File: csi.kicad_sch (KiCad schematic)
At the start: 61 parts, among them J10 Conn_FFC_WE_68715014522, J11 Conn_FFC_WE_68715014522, U43 PI4MSD5V9548AZDEX, U44 AP22615A_TSOT26, U45 AP22615A_TSOT26, U46 AP22615A_TSOT26, U47 AP22615A_TSOT26, U48 NTS0102_XSON, U49 NTS0102_XSON

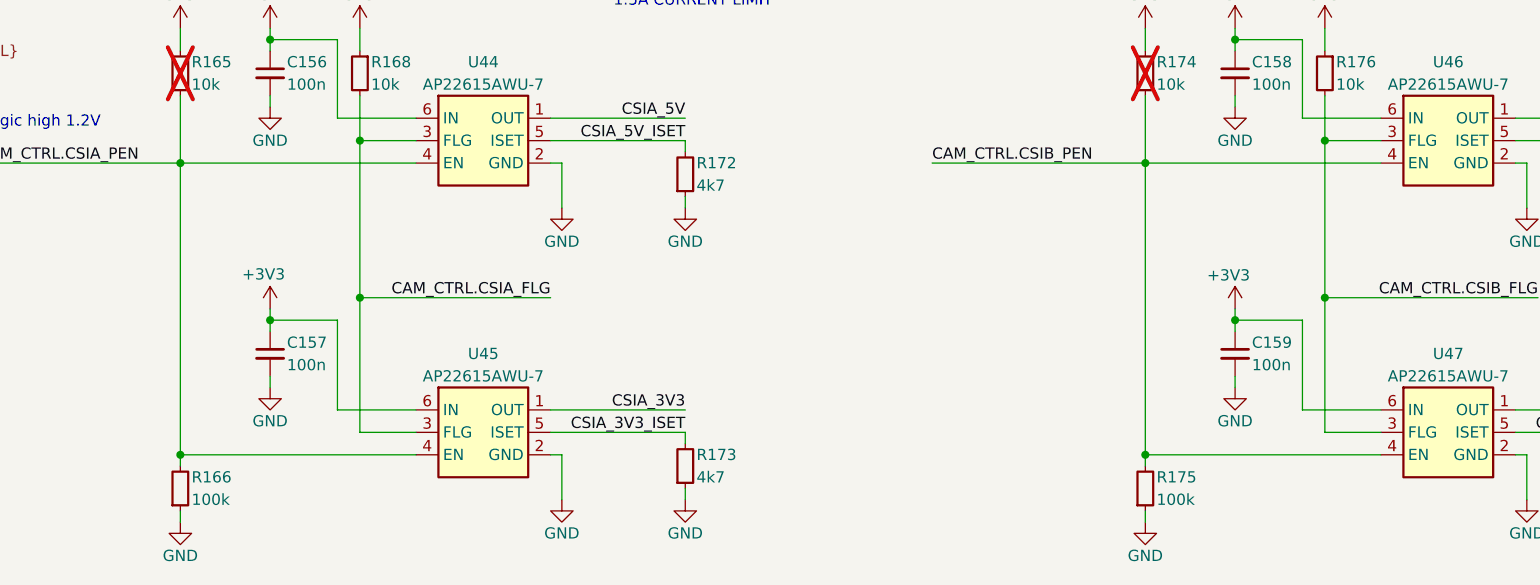
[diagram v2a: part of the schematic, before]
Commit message: [#83396] Implement small post review fixes eg. correct LED resistor values, update sheet table, delete four wire connections
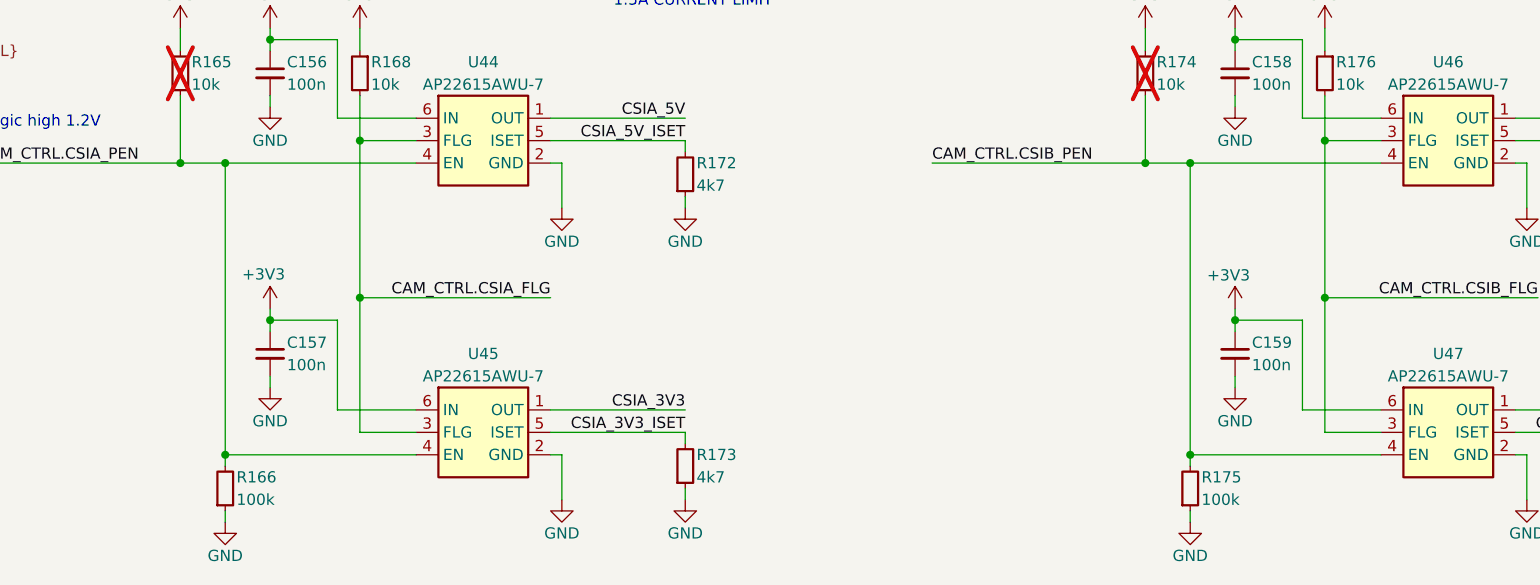
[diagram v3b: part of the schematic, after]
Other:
- moved on the sheet: R166, R175
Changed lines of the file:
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@@
 	)
 	(junction
-		(at 201.93 248.92)
+		(at 207.01 248.92)
 		(diameter 0)
 		(color 0 0 0 0)
@@
 	)
 	(junction
+		(at 97.79 215.9)
+		(diameter 0)
+		(color 0 0 0 0)
+	)
+	(junction
 		(at 349.25 154.94)
 		(diameter 0)
@@
 	)
 	(junction
-		(at 92.71 248.92)
+		(at 97.79 248.92)
 		(diameter 0)
 		(color 0 0 0 0)
@@
 	)
 	(junction
+		(at 207.01 215.9)
+		(diameter 0)
+		(color 0 0 0 0)
+	)
+	(junction
 		(at 284.48 106.68)
 		(diameter 0)
@@
 	(wire
 		(pts
-			(xy 201.93 215.9) (xy 201.93 248.92)
+			(xy 207.01 215.9) (xy 207.01 248.92)
 		)
 		(stroke
@@
 	(wire
 		(pts
-			(xy 92.71 255.27) (xy 92.71 256.54)
+			(xy 97.79 255.27) (xy 97.79 256.54)
 		)
 		(stroke
@@
 	(wire
 		(pts
-			(xy 92.71 215.9) (xy 119.38 215.9)
-		)
-		(stroke
-			(width 0)
-			(type default)
-		)
-	)
-	(wire
-		(pts
 			(xy 102.87 200.66) (xy 102.87 201.93)
 		)
@@
 	(wire
 		(pts
-			(xy 201.93 255.27) (xy 201.93 256.54)
+			(xy 207.01 255.27) (xy 207.01 256.54)
 		)
 		(stroke
@@
 	(wire
 		(pts
-			(xy 92.71 215.9) (xy 92.71 248.92)
+			(xy 97.79 215.9) (xy 97.79 248.92)
 		)
 		(stroke
@@
 	(wire
 		(pts
-			(xy 201.93 248.92) (xy 228.6 248.92)
+			(xy 207.01 215.9) (xy 228.6 215.9)
+		)
+		(stroke
+			(width 0)
+			(type default)
+		)
+	)
+	(wire
+		(pts
+			(xy 207.01 248.92) (xy 228.6 248.92)
 		)
 		(stroke
@@
 	(wire
 		(pts
-			(xy 92.71 248.92) (xy 119.38 248.92)
+			(xy 97.79 248.92) (xy 119.38 248.92)
 		)
 		(stroke
@@
 	(wire
 		(pts
-			(xy 201.93 215.9) (xy 228.6 215.9)
+			(xy 201.93 215.9) (xy 207.01 215.9)
 		)
 		(stroke
@@
 	(wire
 		(pts
+			(xy 97.79 215.9) (xy 119.38 215.9)
+		)
+		(stroke
+			(width 0)
+			(type default)
+		)
+	)
+	(wire
+		(pts
 			(xy 372.11 226.06) (xy 372.11 227.33)
 		)
@@
 	(wire
 		(pts
-			(xy 92.71 248.92) (xy 92.71 250.19)
+			(xy 97.79 248.92) (xy 97.79 250.19)
 		)
 		(stroke
@@
 	(wire
 		(pts
-			(xy 201.93 248.92) (xy 201.93 250.19)
+			(xy 207.01 248.92) (xy 207.01 250.19)
 		)
 		(stroke
@@
 		)
 	)
+	(wire
+		(pts
+			(xy 97.79 215.9) (xy 92.71 215.9)
+		)
+		(stroke
+			(width 0)
+			(type default)
+		)
+	)
 	(bus
 		(pts
@@
 	(symbol
 		(lib_id "antmicroResistors0402:R_100k_0402")
-		(at 92.71 255.27 90)
+		(at 97.79 255.27 90)
 		(unit 1)
 		(exclude_from_sim no)
@@
 		(dnp no)
 		(property "Reference" "R166"
-			(at 93.98 251.46 90)
+			(at 99.06 251.46 90)
 			(effects
 				(font
@@
 		)
 		(property "Value" "R_100k_0402"
-			(at 105.41 234.95 0)
+			(at 110.49 234.95 0)
 			(effects
 				(font
@@
 		)
 		(property "Footprint" "antmicro-footprints:R_0402_1005Metric"
-			(at 107.95 234.95 0)
+			(at 113.03 234.95 0)
 			(effects
 				(font
@@
 		)
 		(property "Datasheet" "https://www.bourns.com/docs/product-datasheets/cr.pdf"
-			(at 110.49 234.95 0)
+			(at 115.57 234.95 0)
 			(effects
 				(font
@@
 		)
 		(property "Description" "SMD Chip Resistor, 100 kohm, ± 1%, 62.5 mW, 0402 [1005 Metric], Thick Film, General Purpose"
-			(at 92.71 255.27 0)
+			(at 97.79 255.27 0)
 			(effects
 				(font
@@
 		)
 		(property "Manufacturer" "Bourns"
-			(at 115.57 234.95 0)
+			(at 120.65 234.95 0)
 			(effects
 				(font
@@
 		)
 		(property "MPN" "CR0402-FX-1003GLF"
-			(at 113.03 234.95 0)
+			(at 118.11 234.95 0)
 			(effects
 				(font
@@
 		)
 		(property "Val" "100k"
-			(at 93.98 254 90)
+			(at 99.06 254 90)
 			(effects
 				(font
@@
 		)
 		(property "License" "Apache-2.0"
-			(at 118.11 234.95 0)
+			(at 123.19 234.95 0)
 			(effects
 				(font
@@
 		)
 		(property "Author" "Antmicro"
-			(at 120.65 234.95 0)
+			(at 125.73 234.95 0)
 			(effects
 				(font
@@
 		)
 		(property "Tolerance" "1%"
-			(at 102.87 234.95 0)
+			(at 107.95 234.95 0)
 			(effects
 				(font
@@
 	(symbol
 		(lib_id "antmicropower:GND")
-		(at 92.71 256.54 0)
+		(at 97.79 256.54 0)
 		(unit 1)
 		(exclude_from_sim no)
@@
 		(dnp no)
 		(property "Reference" "#PWR0292"
-			(at 92.71 262.89 0)
+			(at 97.79 262.89 0)
 			(effects
 				(font
@@
 		)
 		(property "Value" "GND"
-			(at 92.71 260.35 0)
+			(at 97.79 260.35 0)
 			(effects
 				(font
@@
 		)
 		(property "Footprint" ""
-			(at 101.6 264.16 0)
+			(at 106.68 264.16 0)
 			(effects
 				(font
@@
 		)
 		(property "Datasheet" ""
-			(at 101.6 269.24 0)
+			(at 106.68 269.24 0)
 			(effects
 				(font
@@
 		)
 		(property "Description" ""
-			(at 92.71 256.54 0)
+			(at 97.79 256.54 0)
 			(effects
 				(font
@@
 		)
 		(property "Author" "Antmicro"
-			(at 101.6 264.16 0)
+			(at 106.68 264.16 0)
 			(effects
 				(font
@@
 		)
 		(property "License" "Apache-2.0"
-			(at 101.6 266.7 0)
+			(at 106.68 266.7 0)
 			(effects
 				(font
@@
 	(symbol
 		(lib_id "antmicroResistors0402:R_100k_0402")
-		(at 201.93 255.27 90)
+		(at 207.01 255.27 90)
 		(unit 1)
 		(exclude_from_sim no)
@@
 		(dnp no)
 		(property "Reference" "R175"
-			(at 203.2 251.46 90)
+			(at 208.28 251.46 90)
 			(effects
 				(font
@@
 		)
 		(property "Value" "R_100k_0402"
-			(at 214.63 234.95 0)
+			(at 219.71 234.95 0)
 			(effects
 				(font
@@
 		)
 		(property "Footprint" "antmicro-footprints:R_0402_1005Metric"
-			(at 217.17 234.95 0)
+			(at 222.25 234.95 0)
 			(effects
 				(font
@@
 		)
 		(property "Datasheet" "https://www.bourns.com/docs/product-datasheets/cr.pdf"
-			(at 219.71 234.95 0)
+			(at 224.79 234.95 0)
 			(effects
 				(font
@@
 		)
 		(property "Description" "SMD Chip Resistor, 100 kohm, ± 1%, 62.5 mW, 0402 [1005 Metric], Thick Film, General Purpose"
-			(at 201.93 255.27 0)
+			(at 207.01 255.27 0)
 			(effects
 				(font
@@
 		)
 		(property "Manufacturer" "Bourns"
-			(at 224.79 234.95 0)
+			(at 229.87 234.95 0)
 			(effects
 				(font
@@
 		)
 		(property "MPN" "CR0402-FX-1003GLF"
-			(at 222.25 234.95 0)
+			(at 227.33 234.95 0)
 			(effects
 				(font
@@
 		)
 		(property "Val" "100k"
-			(at 203.2 254 90)
+			(at 208.28 254 90)
 			(effects
 				(font
@@
 		)
 		(property "License" "Apache-2.0"
-			(at 227.33 234.95 0)
+			(at 232.41 234.95 0)
 			(effects
 				(font
@@
 		)
 		(property "Author" "Antmicro"
-			(at 229.87 234.95 0)
+			(at 234.95 234.95 0)
 			(effects
 				(font
@@
 		)
 		(property "Tolerance" "1%"
-			(at 212.09 234.95 0)
+			(at 217.17 234.95 0)
 			(effects
 				(font
@@
 	(symbol
 		(lib_id "antmicropower:GND")
-		(at 201.93 256.54 0)
+		(at 207.01 256.54 0)
 		(unit 1)
 		(exclude_from_sim no)
@@
 		(dnp no)
 		(property "Reference" "#PWR0309"
-			(at 201.93 262.89 0)
+			(at 207.01 262.89 0)
 			(effects
 				(font
@@
 		)
 		(property "Value" "GND"
-			(at 201.93 260.35 0)
+			(at 207.01 260.35 0)
 			(effects
 				(font
@@
 		)
 		(property "Footprint" ""
-			(at 210.82 264.16 0)
+			(at 215.9 264.16 0)
 			(effects
 				(font
@@
 		)
 		(property "Datasheet" ""
-			(at 210.82 269.24 0)
+			(at 215.9 269.24 0)
 			(effects
 				(font
@@
 		)
 		(property "Description" ""
-			(at 201.93 256.54 0)
+			(at 207.01 256.54 0)
 			(effects
 				(font
@@
 		)
 		(property "Author" "Antmicro"
-			(at 210.82 264.16 0)
+			(at 215.9 264.16 0)
 			(effects
 				(font
@@
 		)
 		(property "License" "Apache-2.0"
-			(at 210.82 266.7 0)
+			(at 215.9 266.7 0)
 			(effects
 				(font

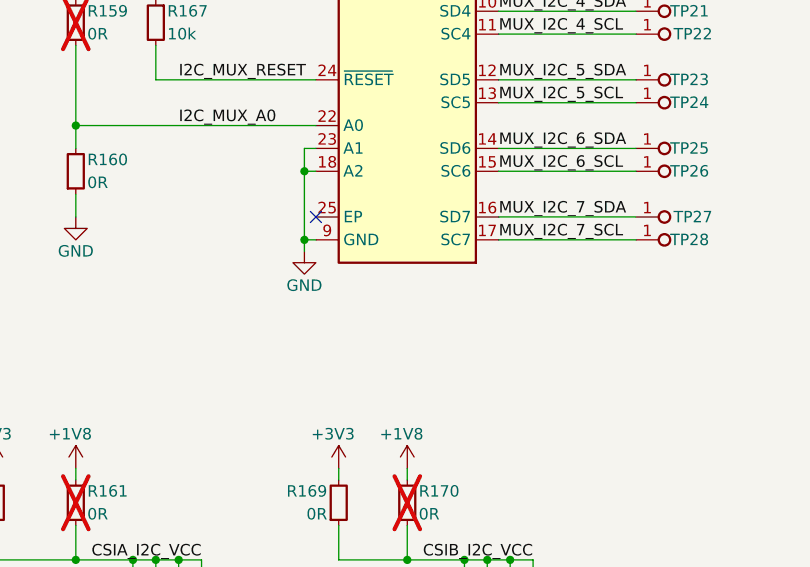
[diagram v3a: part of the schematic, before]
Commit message: [#84355] Add antmicro logo to PCB
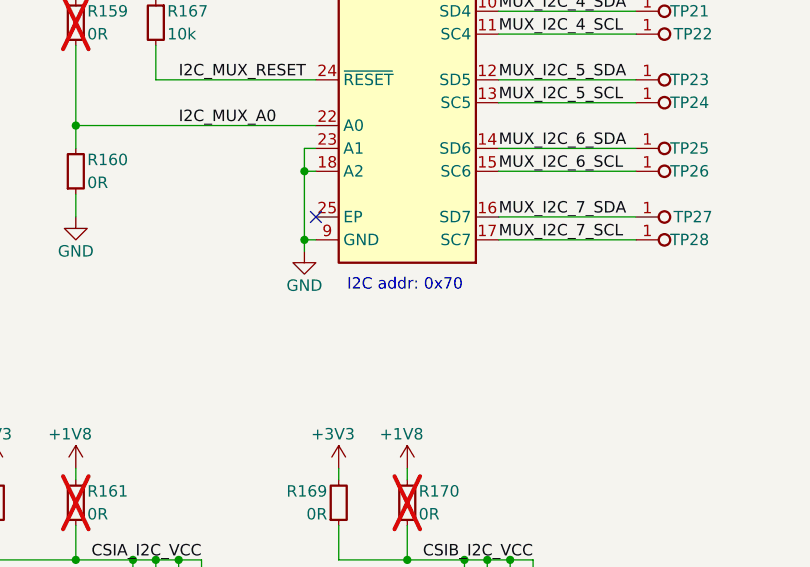
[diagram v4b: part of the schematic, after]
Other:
- note added: "I2C addr: 0x70"
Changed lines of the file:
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@@
+		)
+	)
+	(text "I2C addr: 0x70"
+		(exclude_from_sim no)
+		(at 121.666 114.3 0)
+		(effects
+			(font
+				(size 1.27 1.27)
+			)
 		)
 	)
